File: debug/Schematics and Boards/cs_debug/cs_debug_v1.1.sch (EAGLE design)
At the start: 217 parts, among them J1 J-JTAG-CORTEX_SMD, J19 Solar, J3 HIROSE-DF40_50-PIN_CONNECTORS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, J5 J-WURTH-USBC, Q10 2N7002P, Q3 FDN340P, Q4 2N7002P, Q5 FDN340P, Q6 2N7002P, Q7 FDN340P, Q8 2N7002P, Q9 FDN340P, U1 AP2120N-3.3TRG1, U10 OPA357AIDBVTG4, U11 DAC7574IDGS, U12 MCP73871T-2CCI/ML, U13 USB2412-DZK, U14 INA225AIDGK, U15 OPA357AIDBVTG4, U2 TLV1117LV33DCYR, U204 LOADSWITCH-MIC94164, U3 ESD122DMYR, U5 INA225AIDGK, U6 OPA357AIDBVTG4, U7 INA225AIDGK, U8 OPA357AIDBVTG4, U9 INA225AIDGK, Y1 EPSON_TSX-3225_24.0000MF10Z-C3, Y101 32.768kHz, Y102 12MHz-12pF-K7

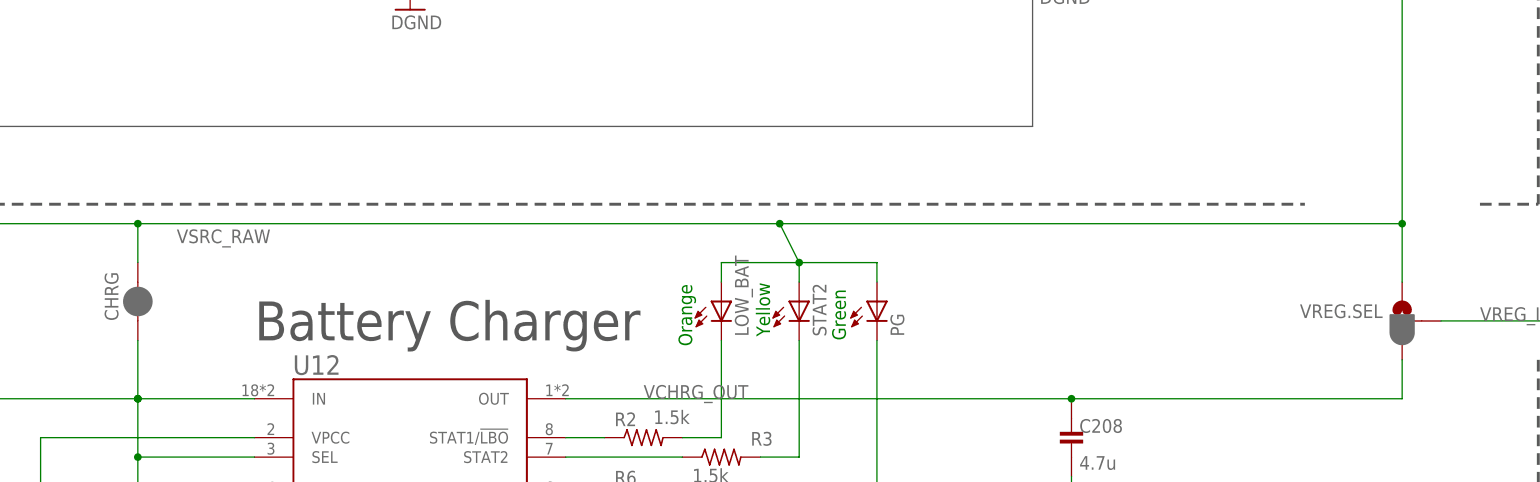
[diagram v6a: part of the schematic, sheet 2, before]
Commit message: DBG: Replace bias resistors of current measurement w/ correct part
And regenerate the CAM files.
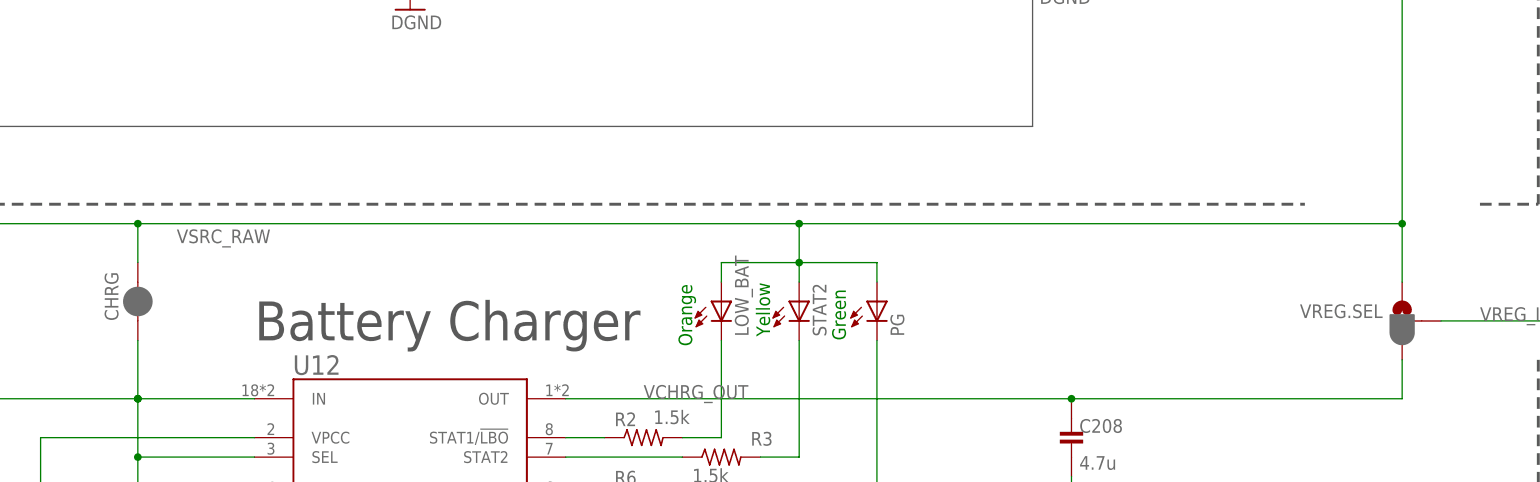
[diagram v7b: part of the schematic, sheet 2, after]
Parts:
- R16, R20, R24, R25, R29, R36, R40, R56: device Resistors:R-0402 -> Resistors:R-0603; MPN ERA-2AEB2491X -> ERA-3AEB2493V; PART_NO ERA-2AEB2491X -> ERA-3AEB2493V
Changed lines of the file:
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@@
 </part>
 <part name="SUPPLY30" library="Supplies" deviceset="+3V3" device=""/>
-<part name="R40" library="Resistors" deviceset="R-" device="0402" value="249k">
-<attribute name="MPN" value="ERA-2AEB2491X"/>
-<attribute name="PART_NO" value="ERA-2AEB2491X"/>
+<part name="R40" library="Resistors" deviceset="R-" device="0603" value="249k">
+<attribute name="MPN" value="ERA-3AEB2493V"/>
+<attribute name="PART_NO" value="ERA-3AEB2493V"/>
 <attribute name="TOL" value="0,1%"/>
 </part>
@@
 <attribute name="TOL" value="0.1%"/>
 </part>
-<part name="R56" library="Resistors" deviceset="R-" device="0402" value="249k">
-<attribute name="MPN" value="ERA-2AEB2491X"/>
-<attribute name="PART_NO" value="ERA-2AEB2491X"/>
+<part name="R56" library="Resistors" deviceset="R-" device="0603" value="249k">
+<attribute name="MPN" value="ERA-3AEB2493V"/>
+<attribute name="PART_NO" value="ERA-3AEB2493V"/>
 <attribute name="TOL" value="0.1%"/>
 </part>
@@
 </part>
 <part name="SUPPLY22" library="Supplies" deviceset="+3V3" device=""/>
-<part name="R24" library="Resistors" deviceset="R-" device="0402" value="249k">
-<attribute name="MPN" value="ERA-2AEB2491X"/>
-<attribute name="PART_NO" value="ERA-2AEB2491X"/>
+<part name="R24" library="Resistors" deviceset="R-" device="0603" value="249k">
+<attribute name="MPN" value="ERA-3AEB2493V"/>
+<attribute name="PART_NO" value="ERA-3AEB2493V"/>
 <attribute name="TOL" value="0,1%"/>
 </part>
@@
 <attribute name="TOL" value="0.1%"/>
 </part>
-<part name="R36" library="Resistors" deviceset="R-" device="0402" value="249k">
-<attribute name="MPN" value="ERA-2AEB2491X"/>
-<attribute name="PART_NO" value="ERA-2AEB2491X"/>
+<part name="R36" library="Resistors" deviceset="R-" device="0603" value="249k">
+<attribute name="MPN" value="ERA-3AEB2493V"/>
+<attribute name="PART_NO" value="ERA-3AEB2493V"/>
 <attribute name="TOL" value="0.1%"/>
 </part>
@@
 </part>
 <part name="SUPPLY19" library="Supplies" deviceset="+3V3" device=""/>
-<part name="R25" library="Resistors" deviceset="R-" device="0402" value="249k">
-<attribute name="MPN" value="ERA-2AEB2491X"/>
-<attribute name="PART_NO" value="ERA-2AEB2491X"/>
+<part name="R25" library="Resistors" deviceset="R-" device="0603" value="249k">
+<attribute name="MPN" value="ERA-3AEB2493V"/>
+<attribute name="PART_NO" value="ERA-3AEB2493V"/>
 <attribute name="TOL" value="0,1%"/>
 </part>
@@
 <attribute name="TOL" value="0.1%"/>
 </part>
-<part name="R29" library="Resistors" deviceset="R-" device="0402" value="249k">
-<attribute name="MPN" value="ERA-2AEB2491X"/>
-<attribute name="PART_NO" value="ERA-2AEB2491X"/>
+<part name="R29" library="Resistors" deviceset="R-" device="0603" value="249k">
+<attribute name="MPN" value="ERA-3AEB2493V"/>
+<attribute name="PART_NO" value="ERA-3AEB2493V"/>
 <attribute name="TOL" value="0.1%"/>
 </part>
@@
 </part>
 <part name="SUPPLY16" library="Supplies" deviceset="+3V3" device=""/>
-<part name="R16" library="Resistors" deviceset="R-" device="0402" value="249k">
-<attribute name="MPN" value="ERA-2AEB2491X"/>
-<attribute name="PART_NO" value="ERA-2AEB2491X"/>
+<part name="R16" library="Resistors" deviceset="R-" device="0603" value="249k">
+<attribute name="MPN" value="ERA-3AEB2493V"/>
+<attribute name="PART_NO" value="ERA-3AEB2493V"/>
 <attribute name="TOL" value="0,1%"/>
 </part>
@@
 <attribute name="TOL" value="0.1%"/>
 </part>
-<part name="R20" library="Resistors" deviceset="R-" device="0402" value="249k">
-<attribute name="MPN" value="ERA-2AEB2491X"/>
-<attribute name="PART_NO" value="ERA-2AEB2491X"/>
+<part name="R20" library="Resistors" deviceset="R-" device="0603" value="249k">
+<attribute name="MPN" value="ERA-3AEB2493V"/>
+<attribute name="PART_NO" value="ERA-3AEB2493V"/>
 <attribute name="TOL" value="0.1%"/>
 </part>
@@
 <net name="VSRC_RAW" class="1">
 <segment>
-<wire x1="241.3" y1="124.46" x2="160.02" y2="124.46" width="0.1524" layer="91"/>
-<wire x1="160.02" y1="124.46" x2="76.2" y2="124.46" width="0.1524" layer="91"/>
+<wire x1="241.3" y1="124.46" x2="162.56" y2="124.46" width="0.1524" layer="91"/>
+<wire x1="162.56" y1="124.46" x2="76.2" y2="124.46" width="0.1524" layer="91"/>
 <junction x="241.3" y="124.46"/>
 <pinref part="VREG.SEL" gate="G$1" pin="1"/>
@@
 <wire x1="76.2" y1="124.46" x2="15.24" y2="124.46" width="0.1524" layer="91"/>
 <wire x1="15.24" y1="124.46" x2="12.7" y2="127" width="0.1524" layer="91"/>
-<junction x="160.02" y="124.46"/>
+<junction x="162.56" y="124.46"/>
 <pinref part="LOW_BAT" gate="G$1" pin="A"/>
-<wire x1="160.02" y1="124.46" x2="162.56" y2="119.38" width="0.1524" layer="91"/>
+<wire x1="162.56" y1="124.46" x2="162.56" y2="119.38" width="0.1524" layer="91"/>
 <wire x1="152.4" y1="116.84" x2="152.4" y2="119.38" width="0.1524" layer="91"/>
 <wire x1="152.4" y1="119.38" x2="162.56" y2="119.38" width="0.1524" layer="91"/>
